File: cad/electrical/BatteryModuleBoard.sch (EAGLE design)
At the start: 11 parts

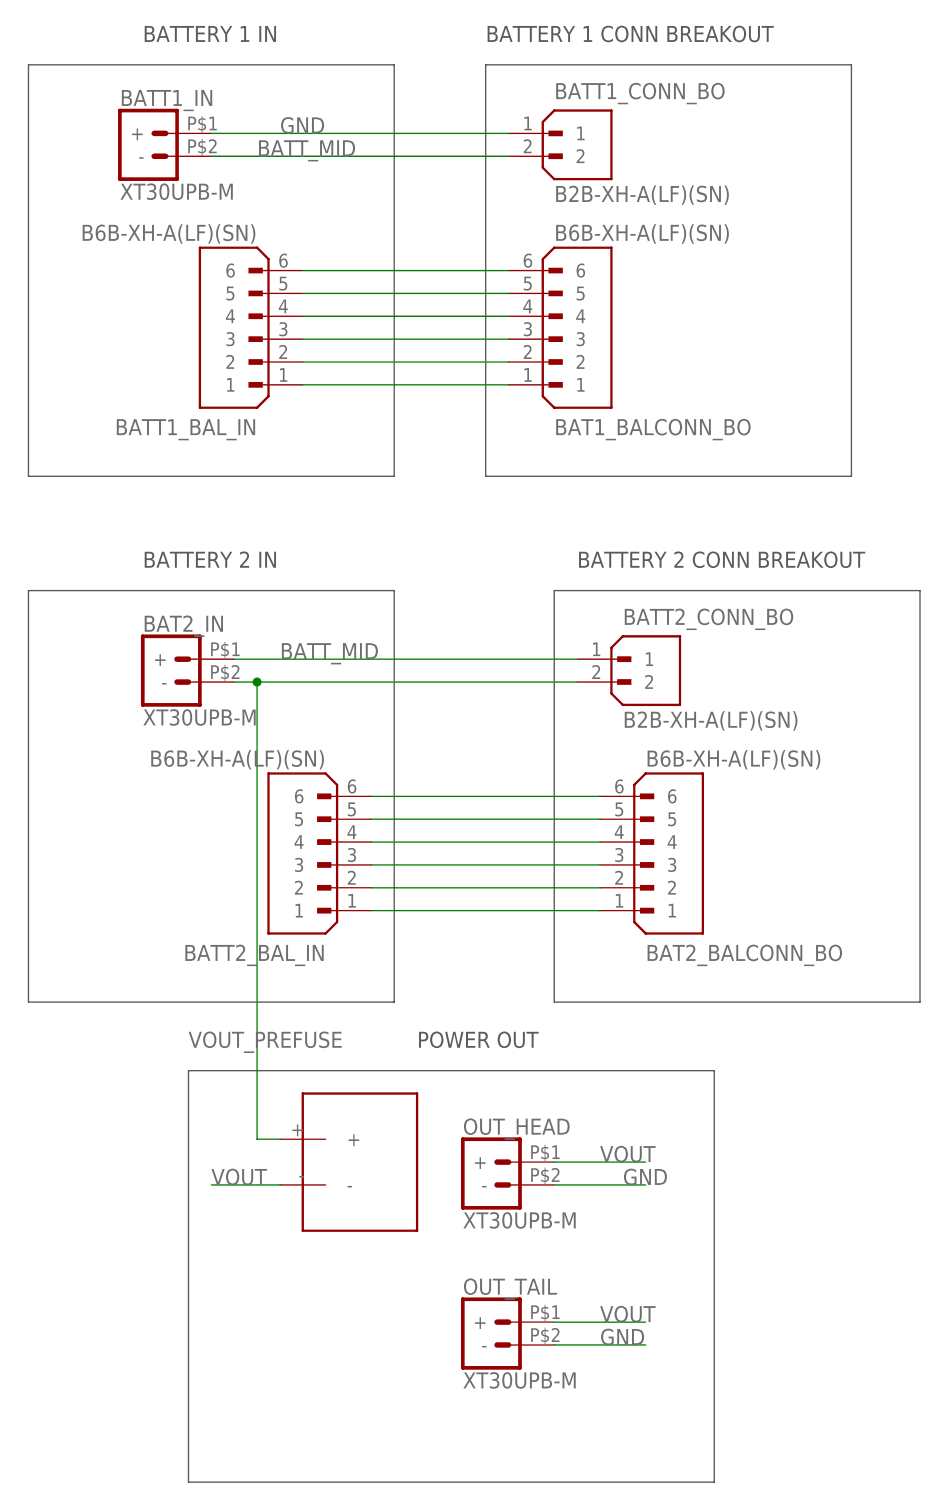
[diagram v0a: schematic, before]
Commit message: Update pcb component sizes and power connections
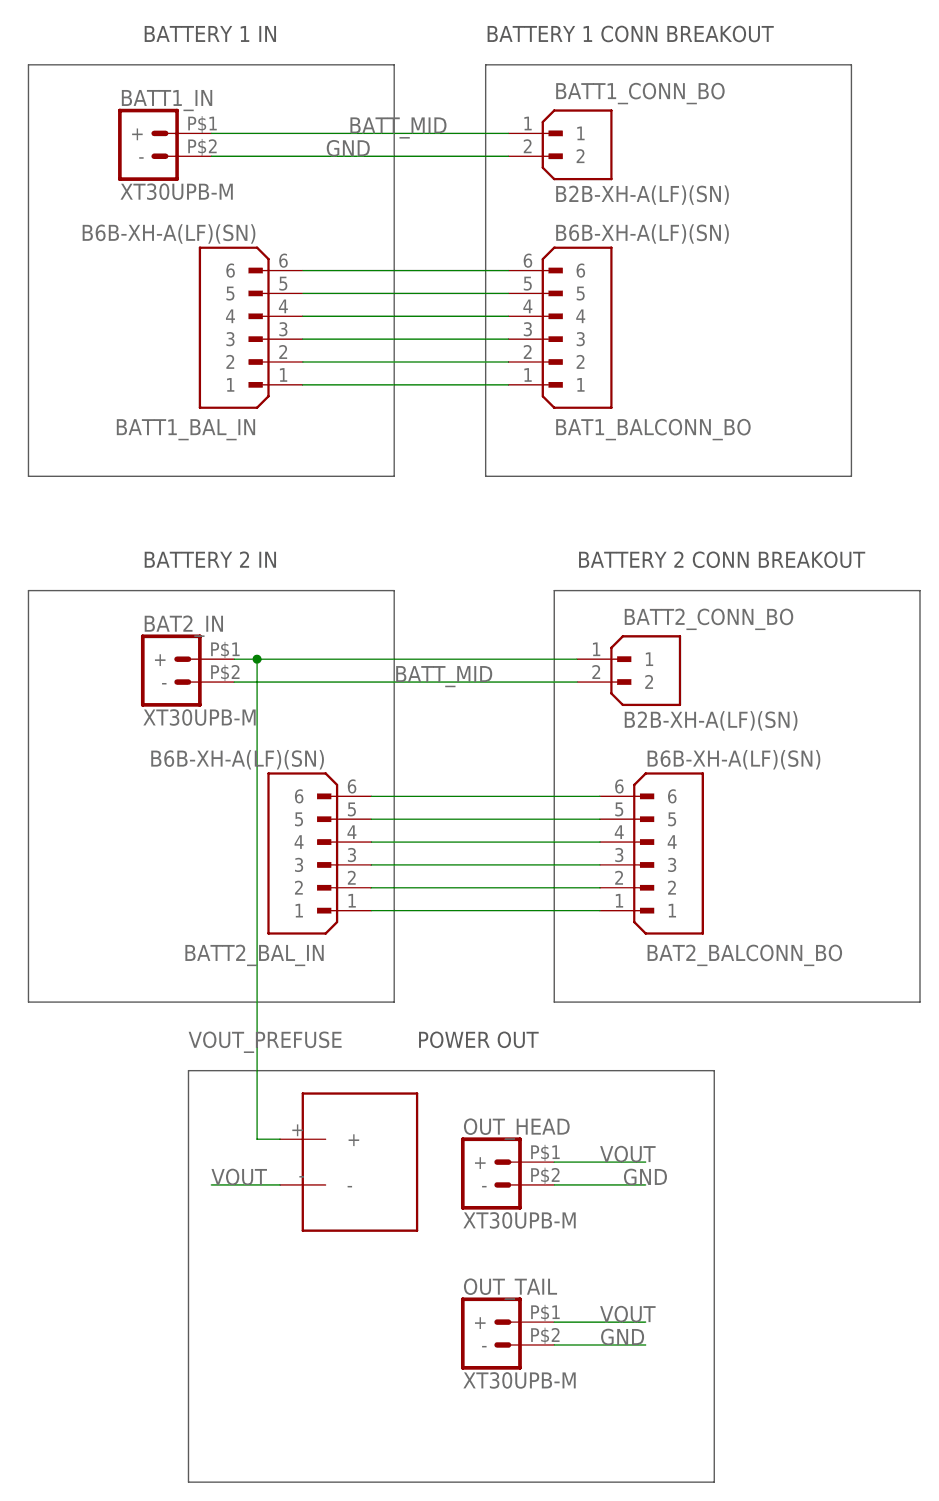
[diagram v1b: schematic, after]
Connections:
- net BATT_MID: now also BAT2_IN.-, BATT1_CONN_BO.1, BATT1_IN.+, BATT2_CONN_BO.2; no longer BAT2_IN.+, BATT1_CONN_BO.2, BATT1_IN.-, BATT2_CONN_BO.1
- net GND: now also BATT1_CONN_BO.2, BATT1_IN.-; no longer BATT1_CONN_BO.1, BATT1_IN.+
- net VOUT_PREFUSE: now also BAT2_IN.+, BATT2_CONN_BO.1; no longer BAT2_IN.-, BATT2_CONN_BO.2
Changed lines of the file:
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@@
 <net name="BATT_MID" class="0">
 <segment>
-<pinref part="BATT1_IN" gate="G$1" pin="-"/>
-<label x="45.72" y="157.48" size="1.778" layer="95"/>
-<pinref part="BATT1_CONN_BO" gate="G$1" pin="2"/>
-<wire x1="40.64" y1="157.48" x2="73.66" y2="157.48" width="0.1524" layer="91"/>
+<pinref part="BATT1_IN" gate="G$1" pin="+"/>
+<pinref part="BATT1_CONN_BO" gate="G$1" pin="1"/>
+<wire x1="40.64" y1="160.02" x2="73.66" y2="160.02" width="0.1524" layer="91"/>
+<label x="55.88" y="160.02" size="1.778" layer="95"/>
 </segment>
 <segment>
-<pinref part="BAT2_IN" gate="G$1" pin="+"/>
-<label x="48.26" y="101.6" size="1.778" layer="95"/>
-<pinref part="BATT2_CONN_BO" gate="G$1" pin="1"/>
-<wire x1="43.18" y1="101.6" x2="81.28" y2="101.6" width="0.1524" layer="91"/>
+<pinref part="BAT2_IN" gate="G$1" pin="-"/>
+<pinref part="BATT2_CONN_BO" gate="G$1" pin="2"/>
+<wire x1="43.18" y1="99.06" x2="81.28" y2="99.06" width="0.1524" layer="91"/>
+<label x="60.96" y="99.06" size="1.778" layer="95"/>
 </segment>
 </net>
 <net name="GND" class="0">
-<segment>
-<pinref part="BATT1_IN" gate="G$1" pin="+"/>
-<label x="48.26" y="160.02" size="1.778" layer="95"/>
-<pinref part="BATT1_CONN_BO" gate="G$1" pin="1"/>
-<wire x1="40.64" y1="160.02" x2="73.66" y2="160.02" width="0.1524" layer="91"/>
-</segment>
 <segment>
 <pinref part="OUT_HEAD" gate="G$1" pin="-"/>
@@
 <wire x1="78.74" y1="25.4" x2="88.9" y2="25.4" width="0.1524" layer="91"/>
 <label x="83.82" y="25.4" size="1.778" layer="95"/>
+</segment>
+<segment>
+<pinref part="BATT1_IN" gate="G$1" pin="-"/>
+<pinref part="BATT1_CONN_BO" gate="G$1" pin="2"/>
+<wire x1="40.64" y1="157.48" x2="73.66" y2="157.48" width="0.1524" layer="91"/>
+<label x="53.34" y="157.48" size="1.778" layer="95"/>
 </segment>
 </net>
@@
 <net name="VOUT_PREFUSE" class="0">
 <segment>
-<pinref part="BAT2_IN" gate="G$1" pin="-"/>
-<wire x1="43.18" y1="99.06" x2="45.72" y2="99.06" width="0.1524" layer="91"/>
-<wire x1="45.72" y1="99.06" x2="45.72" y2="48.26" width="0.1524" layer="91"/>
+<wire x1="45.72" y1="101.6" x2="45.72" y2="48.26" width="0.1524" layer="91"/>
 <wire x1="45.72" y1="48.26" x2="48.26" y2="48.26" width="0.1524" layer="91"/>
 <pinref part="FUSE" gate="G$1" pin="+"/>
-<pinref part="BATT2_CONN_BO" gate="G$1" pin="2"/>
-<wire x1="45.72" y1="99.06" x2="81.28" y2="99.06" width="0.1524" layer="91"/>
-<junction x="45.72" y="99.06"/>
 <label x="38.1" y="58.42" size="1.778" layer="95"/>
+<pinref part="BAT2_IN" gate="G$1" pin="+"/>
+<pinref part="BATT2_CONN_BO" gate="G$1" pin="1"/>
+<wire x1="43.18" y1="101.6" x2="45.72" y2="101.6" width="0.1524" layer="91"/>
+<wire x1="45.72" y1="101.6" x2="81.28" y2="101.6" width="0.1524" layer="91"/>
+<junction x="45.72" y="101.6"/>
 </segment>
 </net>
